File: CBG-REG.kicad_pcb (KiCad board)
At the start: 2 copper layers, 19.5 x 19.5 mm, 37 parts, among them J1 Conn_01x09_Socket, J2 Conn_01x09_Socket, U1 AD8560ACP-REEL7, U2 AD8560ACP-REEL7, U4 74LVC2G04

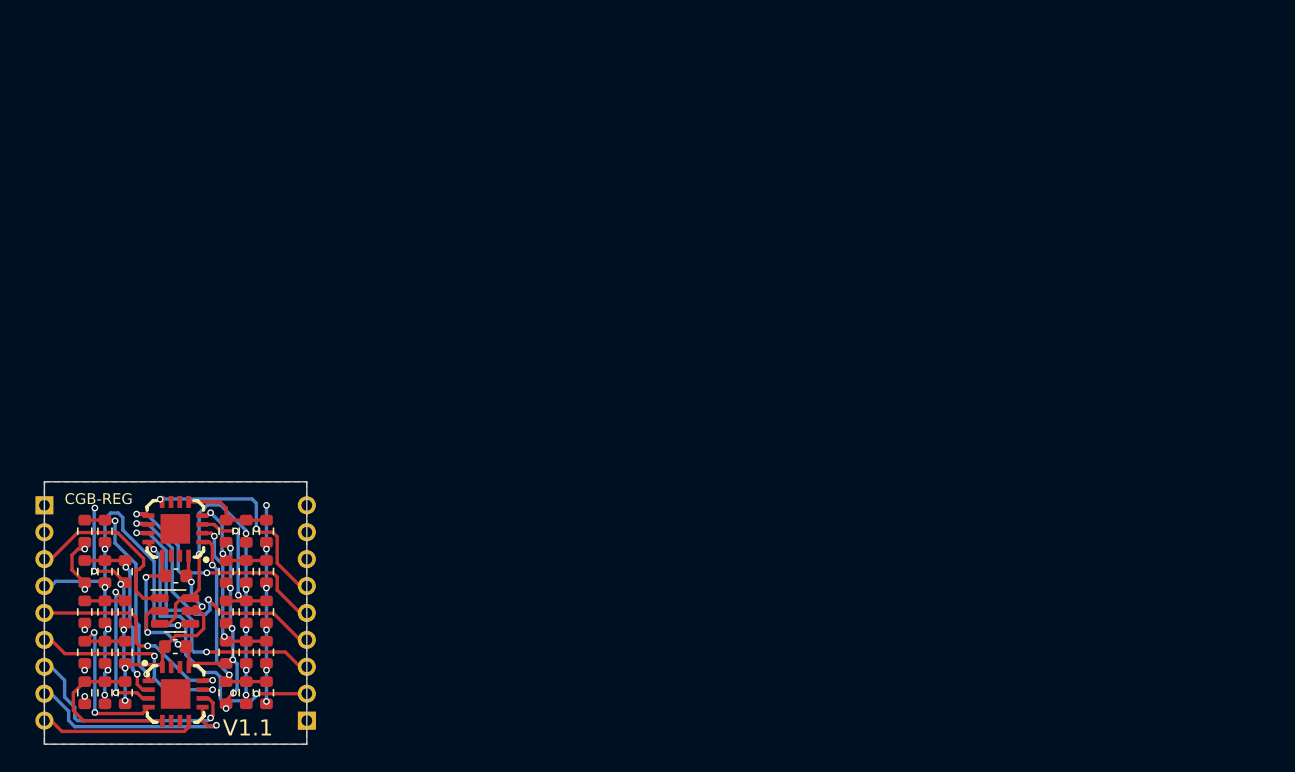
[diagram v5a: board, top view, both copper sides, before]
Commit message: feat: Redesign the board to use an IC that JLCPCB has in stock
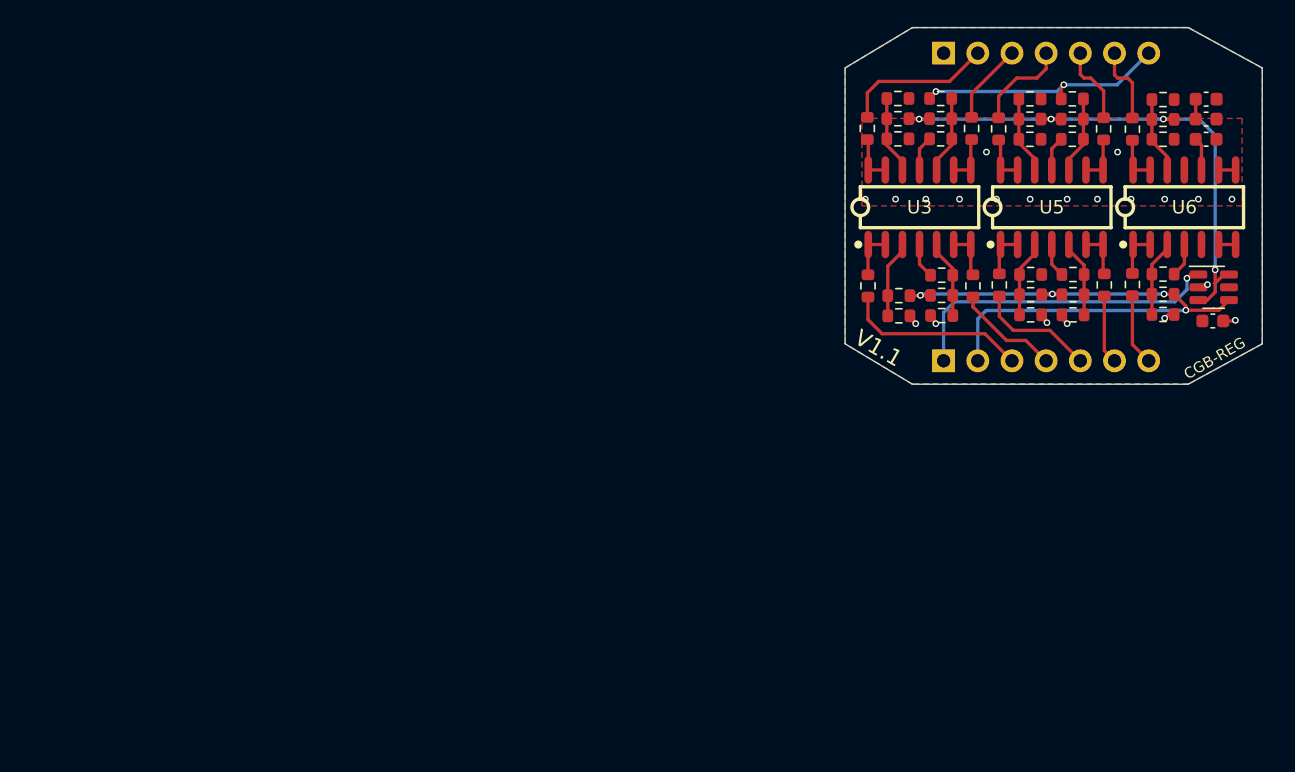
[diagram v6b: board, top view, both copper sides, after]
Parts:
- removed U1, U2: AD8560ACP-REEL7, easyeda2kicad:LFCSP-16_L4.0-W4.0-P0.65-TL-EP2.2
- added C1: 1uF, Capacitor_SMD:C_0603_1608Metric, F.Cu at (166.8, 93.8)
- added C4: 1uF, Capacitor_SMD:C_0603_1608Metric, F.Cu at (166.8, 95.3)
- added R30: 10, Resistor_SMD:R_0603_1608Metric, F.Cu at (149.5, 106.2)
- added R31: 10, Resistor_SMD:R_0603_1608Metric, F.Cu at (149.4, 94.5)
- added R32: 10, Resistor_SMD:R_0603_1608Metric, F.Cu at (141.7, 94.5)
- added R33: 10, Resistor_SMD:R_0603_1608Metric, F.Cu at (151.4, 94.5)
- added R34: 10, Resistor_SMD:R_0603_1608Metric, F.Cu at (159.2, 94.5)
- added R35: 10, Resistor_SMD:R_0603_1608Metric, F.Cu at (141.7, 106.2)
- added R36: 10, Resistor_SMD:R_0603_1608Metric, F.Cu at (159.3, 106.1)
- added R37: 10, Resistor_SMD:R_0603_1608Metric, F.Cu at (151.5, 106.1)
- added R38: 10, Resistor_SMD:R_0603_1608Metric, F.Cu at (161.3, 94.5)
- added R39: 10, Resistor_SMD:R_0603_1608Metric, F.Cu at (161.3, 106.1)
- added U3: GS8624-SR, easyeda2kicad:SOIC-14_L8.6-W3.9-P1.27-LS6.0-BL, F.Cu at (145.5, 100.3)
- added U5: GS8624-SR, easyeda2kicad:SOIC-14_L8.6-W3.9-P1.27-LS6.0-BL, F.Cu at (155.4, 100.3)
- added U6: GS8624-SR, easyeda2kicad:SOIC-14_L8.6-W3.9-P1.27-LS6.0-BL, F.Cu at (165.2, 100.3)
- J1, J2: value Conn_01x09_Socket -> Conn_01x07; footprint Connector_PinHeader_2.00mm:PinHeader_1x09_P2.00mm_Vertical -> Connector_PinHeader_2.54mm:PinHeader_1x07_P2.54mm_Vertical
- moved C3 86.7 mm to (166.8, 92.3), turned to 180 degrees
- moved R14 84.9 mm to (163.6, 108.3), turned to 0 degrees
- moved R12 84.0 mm to (163.6, 106.8), turned to 0 degrees
- moved R13 83.2 mm to (163.6, 105.3), turned to 180 degrees
- moved U4 80.8 mm to (167.4, 106.3)
- moved C2 79.3 mm to (167.3, 108.8), turned to 0 degrees
- moved R11 77.6 mm to (156.9, 108.3), turned to 180 degrees
- moved R9 76.7 mm to (156.9, 106.8), turned to 180 degrees
- moved R10 75.8 mm to (156.9, 105.3), turned to 0 degrees
- moved R29 75.5 mm to (163.6, 95.3), turned to 0 degrees
- moved J2 74.8 mm to (147.3, 88.9), turned to -90 degrees
- moved R27 74.7 mm to (163.6, 93.8), turned to 0 degrees
- moved R28 73.9 mm to (163.6, 92.3), turned to 180 degrees
- moved R8 73.7 mm to (153.8, 108.3), turned to 0 degrees
- moved R5 72.7 mm to (153.8, 106.8), turned to 0 degrees
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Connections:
- J1 pad 1: GND -> SW_IN
- J1 pad 2: v5 -> SW
- J1 pad 3: v6 -> v0
- J1 pad 4: v7 -> v1
- J1 pad 5: v8 -> v2
- J1 pad 6: v9 -> v3
- J1 pad 7: +5V -> v4
- J2 pad 1: unconnected-(J2-Pin_1-Pad1) -> GND
- J2 pad 2: unconnected-(J2-Pin_2-Pad2) -> v5
- J2 pad 3: SW_IN -> v6
- J2 pad 4: SW -> v7
- J2 pad 5: v0 -> v8
- J2 pad 6: v1 -> v9
- J2 pad 7: v2 -> +5V
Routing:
- net GND: track 38.4 -> 14.7 mm, vias 14 -> 21
- net +5V: track 49.5 -> 26.5 mm, vias 14 -> 2
- net v6: track 21.1 -> 6.01 mm, vias 2 -> 0
- net v7: track 20.3 -> 7.14 mm, vias 2 -> 0
- net SW: track 33.8 -> 45.9 mm, vias 6 -> 4
- net v8: track 17.8 -> 5.81 mm, vias 2 -> 0
- net SW_IN: track 13.3 -> 24.2 mm, vias 0 -> 1
- net v3: track 16.0 -> 5.12 mm, vias 1 -> 0
- net v5: track 21.7 -> 11.3 mm, vias 2 -> 0
- net 'SW: track 30.5 -> 40.8 mm, vias 6 -> 4
- net v9: track 15.6 -> 5.81 mm, vias 2 -> 0
- net V0 Raw: track 15.2 -> 5.75 mm, vias 2 -> 0
- net V5 Raw: track 14.6 -> 5.79 mm, vias 2 -> 0
- net V2 Raw: track 14.1 -> 5.29 mm, vias 2 -> 0
- net V3 Raw: track 14.2 -> 5.70 mm, vias 2 -> 0
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- added copper zone on F.Cu, net GND
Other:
- board size 19.5 x 19.5 mm -> 31 x 26.5 mm
- board text removed: "NC"
